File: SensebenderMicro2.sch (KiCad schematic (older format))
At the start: 31 parts, among them P1 Debug, P2 MYSX_1.2, P3 Antenna, U1 ATSAMD21E, U2 AP1117D33, U3 NRF24L01, U4 RFM69HW, U5 ATSHA204A, U6 AT25DF512C, U7 Si7021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

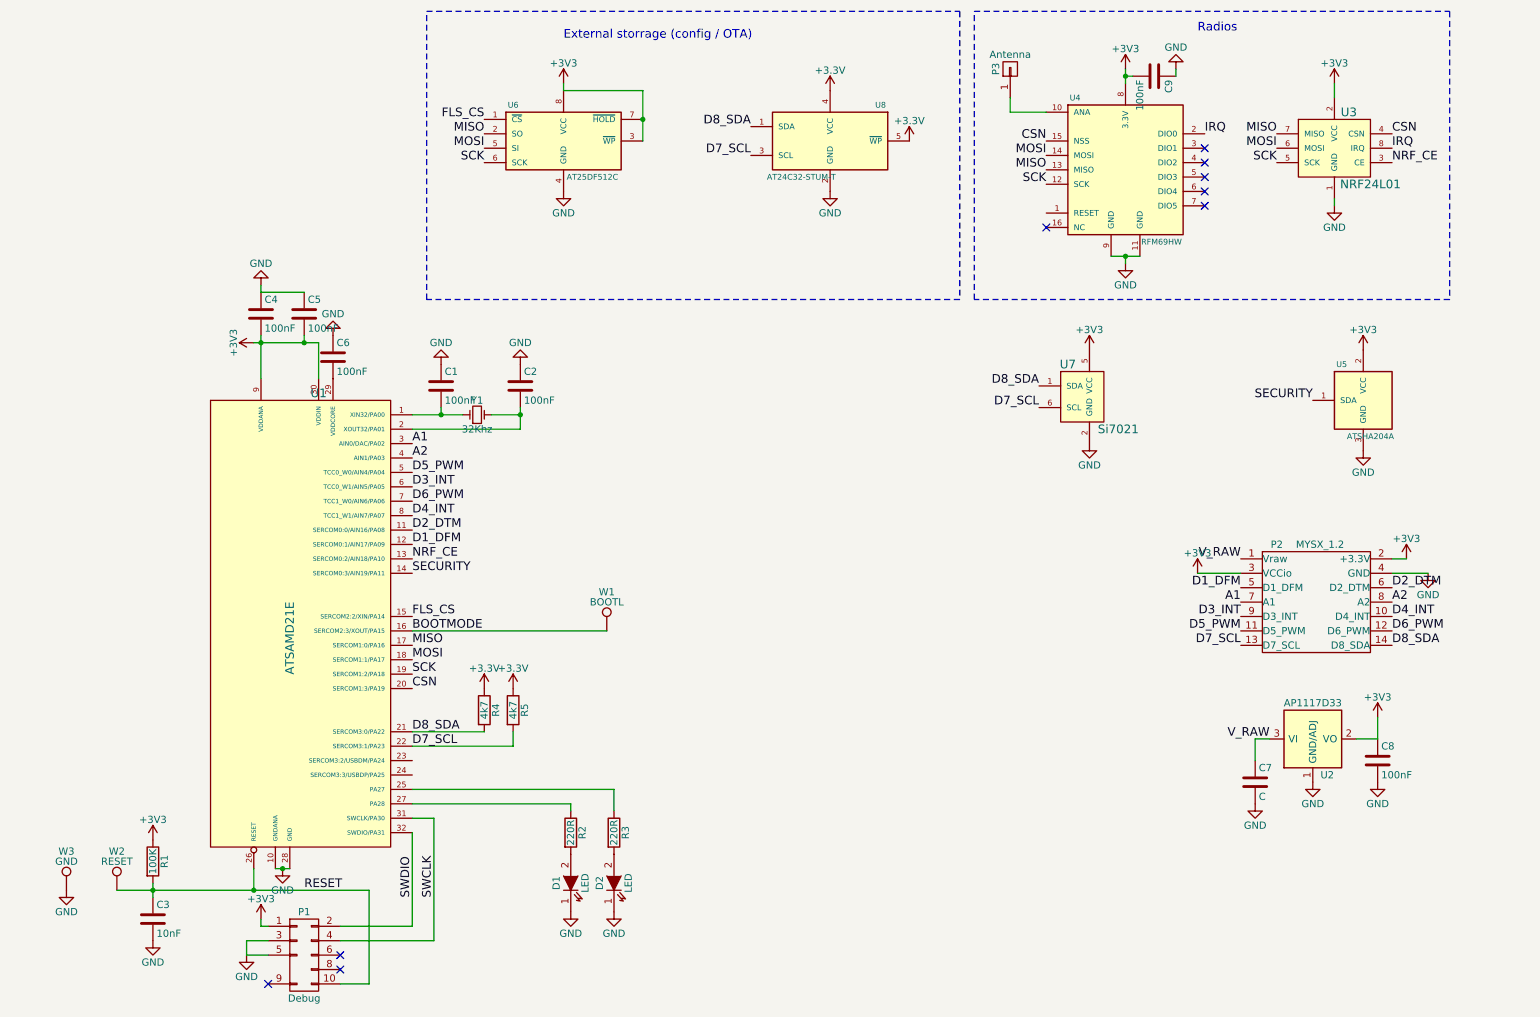
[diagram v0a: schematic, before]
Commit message: Added filtering for analog supply
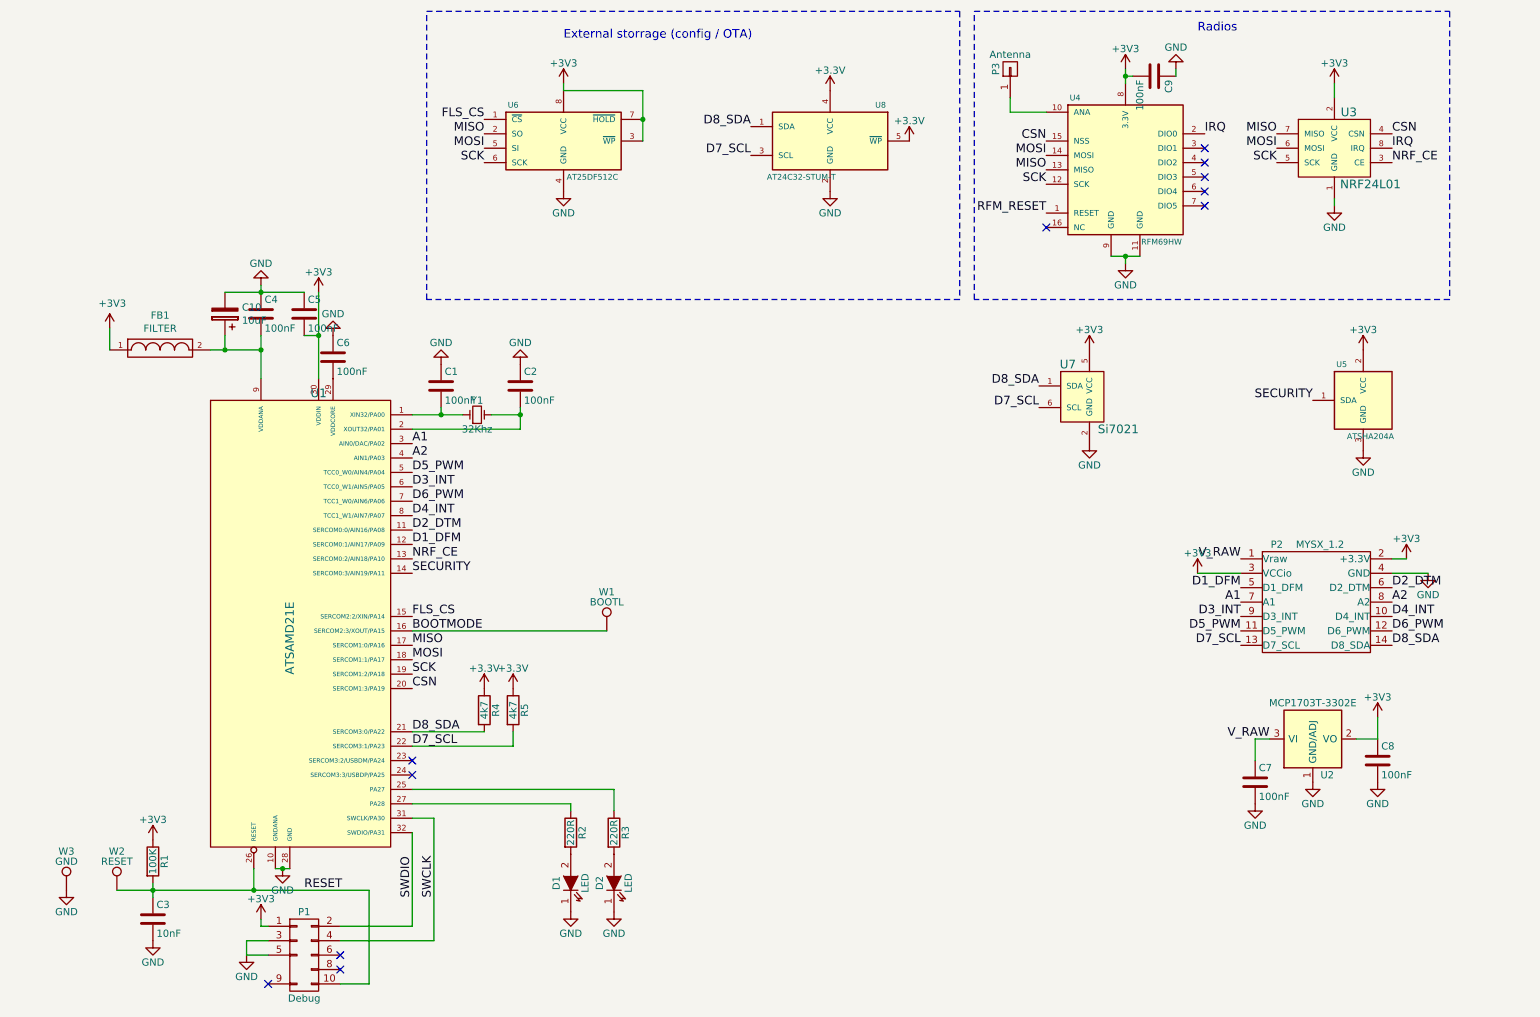
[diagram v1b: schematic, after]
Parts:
- added C10: 10uF, Capacitors_SMD:C_0603, symbol CP
- added FB1: FILTER, Resistors_SMD:R_0603, symbol FILTER
- C7: value C -> 100nF
- U2: value AP1117D33 -> MCP1703T-3302E
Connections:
- net +3V3: now also FB1.1; no longer C4.2, U1.9 (VDDANA)
- net GND: now also C10.2
- net RFM_RESET: now reaches U4.1 (RESET)
- new net: C10.1, C4.2, FB1.2, U1.9 (VDDANA)
- no-connect marks 9 -> 11
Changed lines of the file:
@@
 P 9850 5600
 F 0 "U2" H 9950 5350 50  0000 C CNN
-F 1 "AP1117D33" H 9850 5850 50  0000 C CNN
+F 1 "MCP1703T-3302E" H 9850 5850 50  0000 C CNN
 F 2 "Housings_SOT-23_SOT-143_TSOT-6:SOT-23" H 9850 5600 60  0001 C CNN
 F 3 "" H 9850 5600 60  0000 C CNN
@@
 L +3V3 #PWR05
 U 1 1 55C10285
-P 2500 2850
-F 0 "#PWR05" H 2500 2700 50  0001 C CNN
-F 1 "+3V3" H 2500 2990 50  0000 C CNN
-F 2 "" H 2500 2850 60  0000 C CNN
-F 3 "" H 2500 2850 60  0000 C CNN
-	1    2500 2850
-	0    -1   1    0
+P 2950 2500
+F 0 "#PWR05" H 2950 2350 50  0001 C CNN
+F 1 "+3V3" H 2950 2640 50  0000 C CNN
+F 2 "" H 2950 2500 60  0000 C CNN
+F 3 "" H 2950 2500 60  0000 C CNN
+	1    2950 2500
+	-1   0    0    -1
 $EndComp
 Wire Wire Line
 	2550 2800 2550 3100
-Connection ~ 2550 2850
 $Comp
 L RFM69HW U4
@@
 $EndComp
 Wire Wire Line
-	2500 2850 2950 2850
-Wire Wire Line
-	2950 2850 2950 3100
+	2950 2500 2950 3100
 $Comp
 L C C1
@@
 	1    0    0    -1
 $EndComp
-Wire Wire Line
-	2850 2800 2850 2850
-Connection ~ 2850 2850
 $Comp
 L GND #PWR030
@@
 	2550 2500 2550 2450
 Wire Wire Line
-	2550 2500 2850 2500
+	2300 2500 2850 2500
 Text Label 3600 4850 0    60   ~ 0
 BOOTMODE
@@
 P 9450 5900
 F 0 "C7" H 9475 6000 50  0000 L CNN
-F 1 "C" H 9475 5800 50  0000 L CNN
+F 1 "100nF" H 9475 5800 50  0000 L CNN
 F 2 "Capacitors_SMD:C_0603" H 9488 5750 50  0001 C CNN
 F 3 "" H 9450 5900 50  0000 C CNN
@@
 	1    0    0    -1
 $EndComp
+NoConn ~ 3600 5850
+NoConn ~ 3600 5750
+Text Label 8000 1950 2    60   ~ 0
+RFM_RESET
+$Comp
+L FILTER FB1
+U 1 1 56E87264
+P 1850 2900
+F 0 "FB1" H 1850 3140 50  0000 C CNN
+F 1 "FILTER" H 1850 3049 50  0000 C CNN
+F 2 "Resistors_SMD:R_0603" H 1850 2900 50  0001 C CNN
+F 3 "" H 1850 2900 50  0000 C CNN
+	1    1850 2900
+	1    0    0    -1
+$EndComp
+Wire Wire Line
+	2850 2800 2950 2800
+Connection ~ 2950 2800
+Wire Wire Line
+	2200 2900 2550 2900
+Connection ~ 2550 2900
+$Comp
+L +3V3 #PWR037
+U 1 1 56E87591
+P 1500 2750
+F 0 "#PWR037" H 1500 2600 50  0001 C CNN
+F 1 "+3V3" H 1518 2923 50  0000 C CNN
+F 2 "" H 1500 2750 50  0000 C CNN
+F 3 "" H 1500 2750 50  0000 C CNN
+	1    1500 2750
+	1    0    0    -1
+$EndComp
+Wire Wire Line
+	1500 2750 1500 2900
+$Comp
+L CP C10
+U 1 1 56E8764F
+P 2300 2650
+F 0 "C10" H 2182 2604 50  0000 R CNN
+F 1 "10uF" H 2182 2695 50  0000 R CNN
+F 2 "Capacitors_SMD:C_0603" H 2338 2500 50  0001 C CNN
+F 3 "" H 2300 2650 50  0000 C CNN
+	1    2300 2650
+	-1   0    0    1
+$EndComp
+Wire Wire Line
+	2300 2800 2300 2900
+Connection ~ 2300 2900
+Connection ~ 2550 2500
 $EndSCHEMATC

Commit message: Added fet to switch power to radio / ATSHA
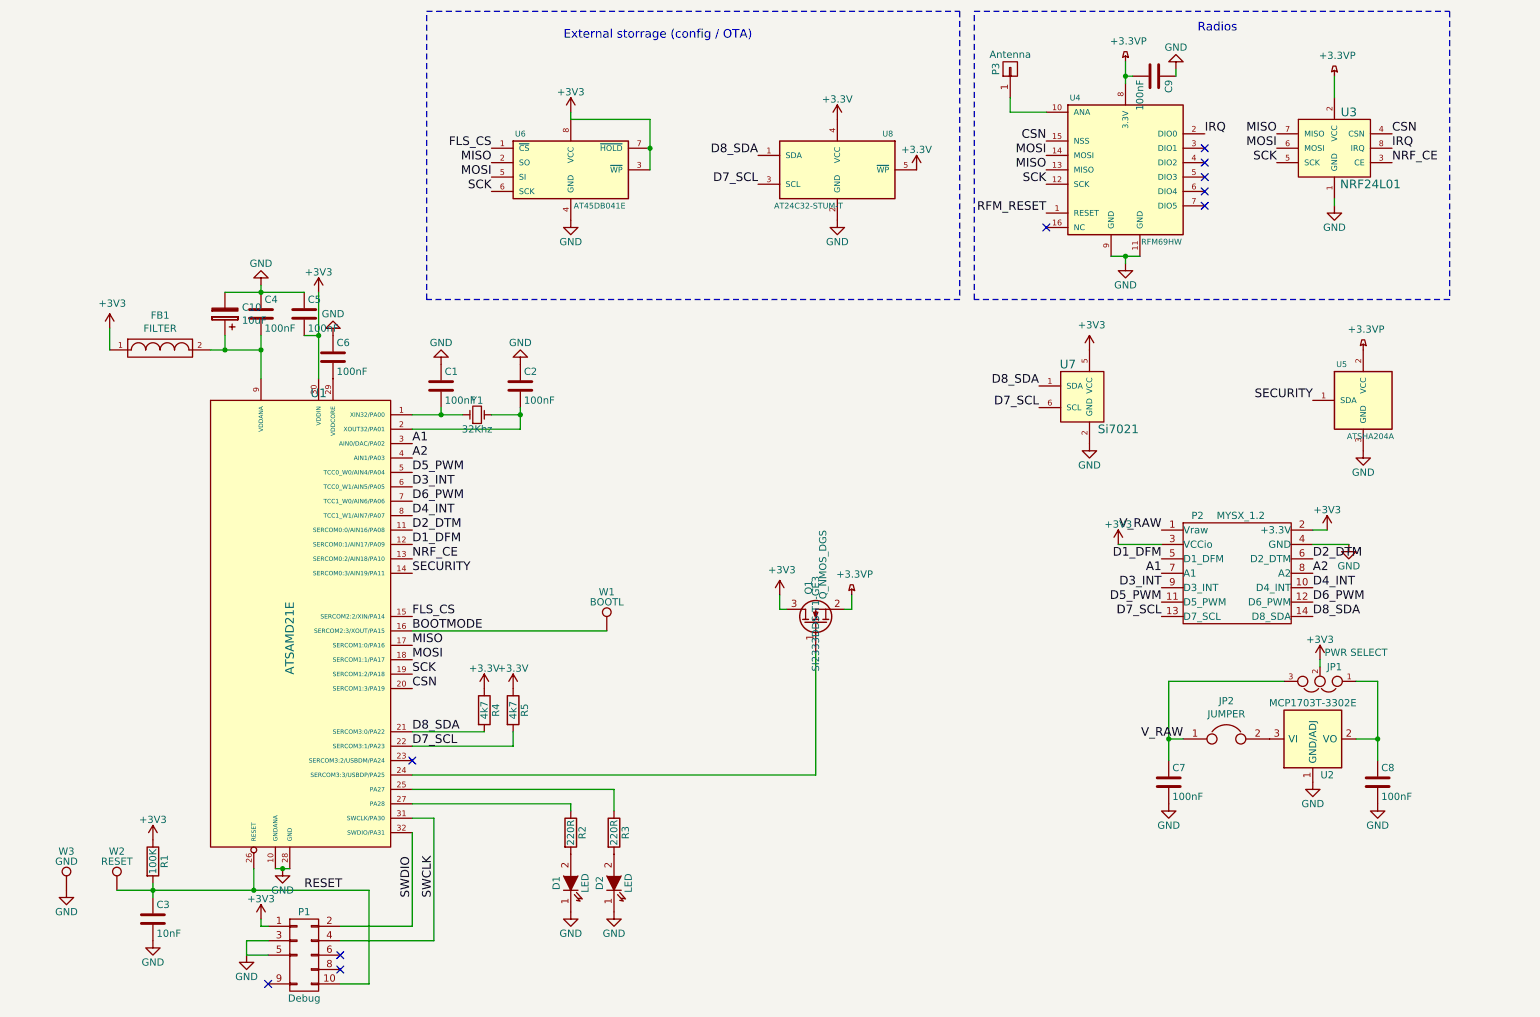
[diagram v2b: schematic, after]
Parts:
- added JP1: PWR SELECT, mysensors_obscurities:3_pin_solder_jumper_smd, symbol JUMPER3
- added JP2: JUMPER, mysensors_obscurities:2_pin_solder_jumper_smd, symbol JUMPER
- added Q1: Q_NMOS_DGS, TO_SOT_Packages_SMD:SOT-23, symbol Q_NMOS_GSD
- U6: value AT25DF512C -> AT45DB041E
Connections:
- net +3V3: now also JP1.2, Q1.3 (D); no longer C8.1, C9.2, U2.2 (VO), U3.2 (VCC), U4.8 (3.3V), U5.2 (VCC)
- net V_RAW: now also JP1.3, JP2.1; no longer U2.3 (VI)
- net at U1.24 (SERCOM3:3/USBDP/PA25): now also Q1.1 (G)
- new net: C8.1, JP1.1, U2.2 (VO)
- new net: JP2.2, U2.3 (VI)
- new net +3.3VP: C9.2, Q1.2 (S), U3.2 (VCC), U4.8 (3.3V), U5.2 (VCC)
- no-connect marks 11 -> 10
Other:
- moved on the sheet: C7, C8, P2, U6, U8

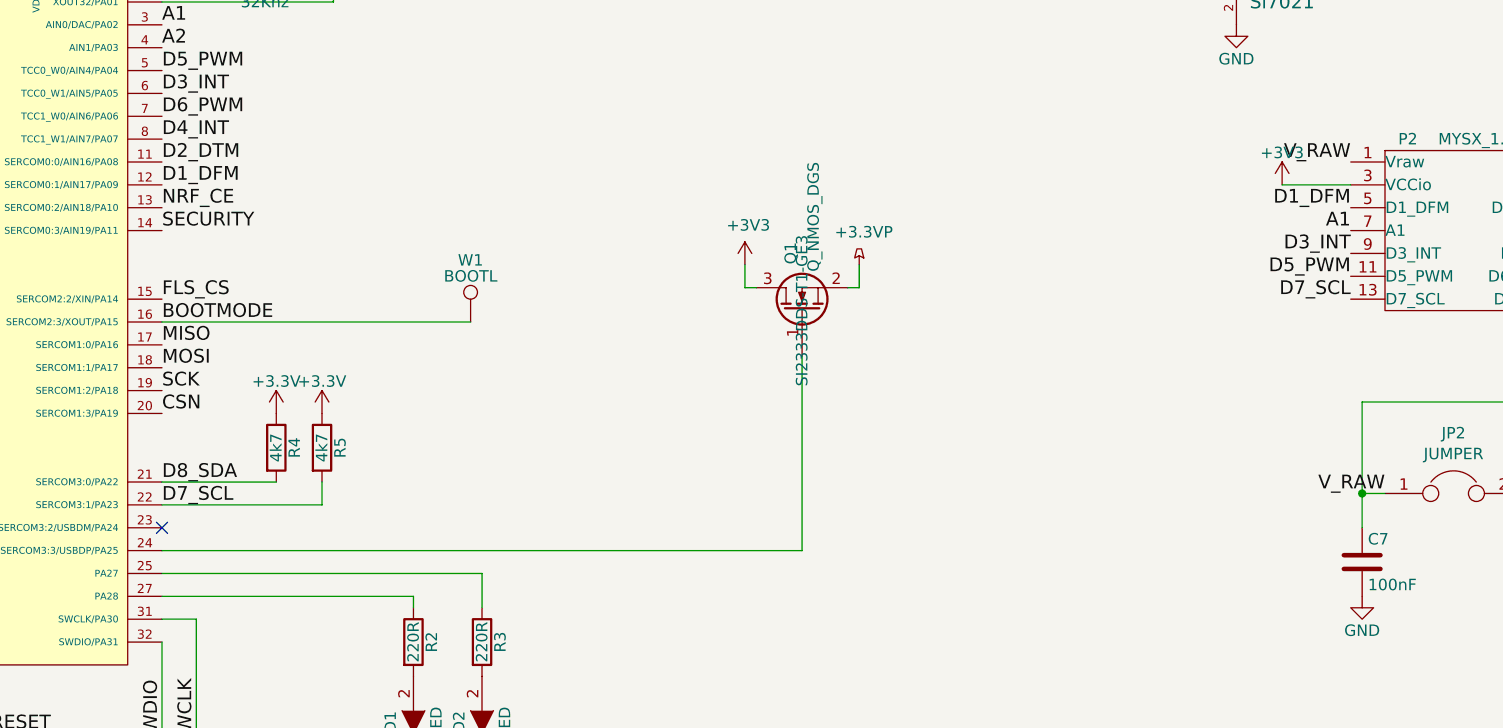
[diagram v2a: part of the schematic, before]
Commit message: Added Gate pull up and series resistor to Q1
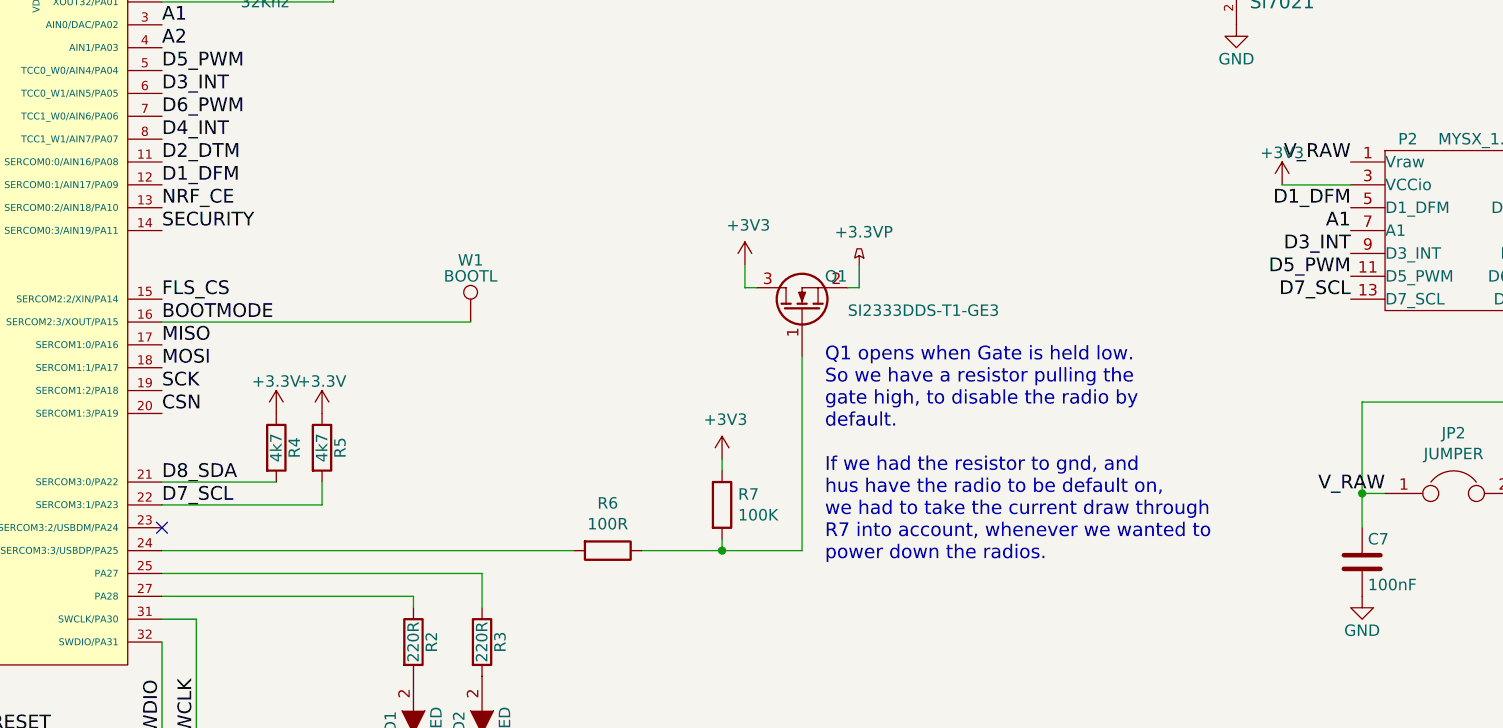
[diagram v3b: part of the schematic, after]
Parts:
- added R6: 100R, Resistors_SMD:R_0603, symbol R
- added R7: 100K, Resistors_SMD:R_0603, symbol R
- Q1: value Q_NMOS_DGS -> SI2333DDS-T1-GE3
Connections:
- net +3V3: now also R7.1
- net at U1.24 (SERCOM3:3/USBDP/PA25): now also R6.2; no longer Q1.1 (G)
- new net: Q1.1 (G), R6.1, R7.2
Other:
- note added: "Q1 opens when Gate is held low. \nSo we have a resistor pulling the \ngate high, to disable the radio by\ndefault.\n\nIf we had the resistor to gnd, and \nhus have the radio to be default on,\nwe had to take the current draw through\nR7 into account, whenever we wanted to\npower down the radios."

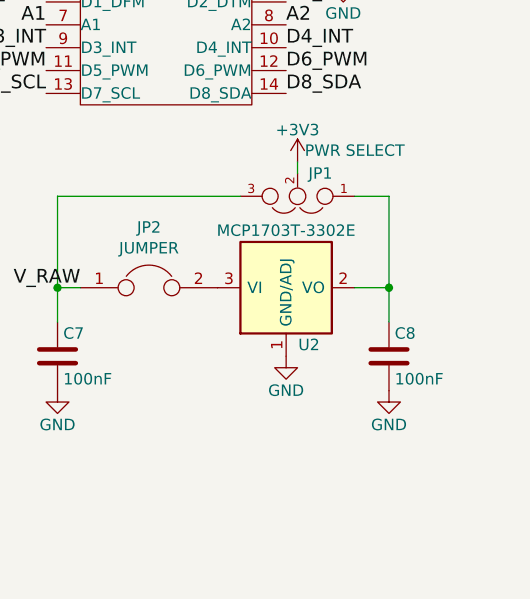
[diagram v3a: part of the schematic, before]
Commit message: Rerouted to make room for GND via at C7
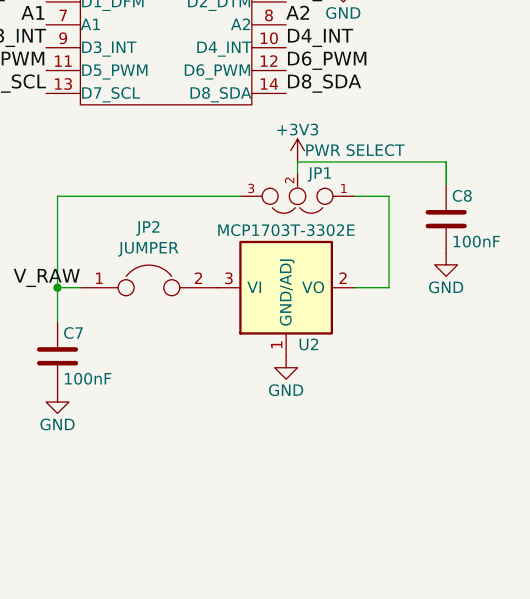
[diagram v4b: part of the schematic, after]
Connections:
- net +3V3: now also C8.1
- net at JP1.1, U2.2 (VO): no longer C8.1
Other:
- moved on the sheet: C8
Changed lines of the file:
@@
 L C C8
 U 1 1 56BA7943
-P 10300 5900
-F 0 "C8" H 10325 6000 50  0000 L CNN
-F 1 "100nF" H 10325 5800 50  0000 L CNN
-F 2 "Capacitors_SMD:C_0603" H 10338 5750 50  0001 C CNN
-F 3 "" H 10300 5900 50  0000 C CNN
-	1    10300 5900
+P 10550 5300
+F 0 "C8" H 10575 5400 50  0000 L CNN
+F 1 "100nF" H 10575 5200 50  0000 L CNN
+F 2 "Capacitors_SMD:C_0603" H 10588 5150 50  0001 C CNN
+F 3 "" H 10550 5300 50  0000 C CNN
+	1    10550 5300
 	1    0    0    -1
 $EndComp
@@
 L GND #PWR029
 U 1 1 56BA7B39
-P 10300 6050
-F 0 "#PWR029" H 10300 5800 50  0001 C CNN
-F 1 "GND" H 10300 5900 50  0000 C CNN
-F 2 "" H 10300 6050 50  0000 C CNN
-F 3 "" H 10300 6050 50  0000 C CNN
-	1    10300 6050
+P 10550 5450
+F 0 "#PWR029" H 10550 5200 50  0001 C CNN
+F 1 "GND" H 10550 5300 50  0000 C CNN
+F 2 "" H 10550 5450 50  0000 C CNN
+F 3 "" H 10550 5450 50  0000 C CNN
+	1    10550 5450
 	1    0    0    -1
 $EndComp
@@
 07 00 85 88 3B 00 28 44 DC 01 40 21 E2 0E 00 0A 11 77 00 50 88 B8 03 80 42 C4 1D 00 14 22 EE 00
 A0 10 71 07 00 85 88 3B 00 28 F4 2F 6E 0E 73 66 69 F5 31 42 00 00 00 00 49 45 4E 44 AE 42 60 82
-78
+B0
 EndData
 $EndBitmap
@@
 	10300 5600 10150 5600
 Wire Wire Line
-	10300 5200 10300 5750
-Wire Wire Line
 	2850 2800 2950 2800
 Connection ~ 2950 2800
@@
 	8850 5200 9650 5200
 Connection ~ 8850 5600
-Connection ~ 10300 5600
 Wire Wire Line
 	6400 5850 5700 5850
@@
 Text Notes 6500 5900 0    60   ~ 0
 Q1 opens when Gate is held low. \nSo we have a resistor pulling the \ngate high, to disable the radio by\ndefault.\n\nIf we had the resistor to gnd, and \nhus have the radio to be default on,\nwe had to take the current draw through\nR7 into account, whenever we wanted to\npower down the radios.
+Wire Wire Line
+	10300 5200 10300 5600
+Wire Wire Line
+	9900 5050 10550 5050
+Wire Wire Line
+	10550 5050 10550 5150
 $EndSCHEMATC
